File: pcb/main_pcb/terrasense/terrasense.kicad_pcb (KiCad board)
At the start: 4 copper layers, 100 x 80 mm, 79 parts, among them J1 SSR 0, J10 12V, J11 OneWire0, J12 12V In, J13 OneWire1, J14 OneWire2, J15 OneWire3, J16 OneWire4, J17 OneWire5, J18 I2C Mult 0, J19 I2C Mult 1, J2 SSR 1, J20 I2C Mult 2, J21 I2C Mult 3, J22 OneWire6, J23 OneWire7, J24 I2C Mult 4, J25 I2C Mult 5, J26 I2C_Debug, J27 ExtraIO, J3 SSR 2, J4 SSR 3, J5 FAN0, J6 FAN1, J7 XKZ-Y25-NPN, J8 SSR 0-3, J9 3V3, Q1 MMBT2222A, Q10 MMBT2222A, Q2 MMBT2222A, Q3 MMBT2222A, Q4 MMBT2222A, Q5 MMBT2222A, Q6 BSS84, Q7 MMBT2222A, Q8 MMBT2222A, Q9 BSS84, U1 ESP32-C6-DevKitC-1, U2 Mini560, U3 TCA9548APWR, U4 MPM3632CGQV-P

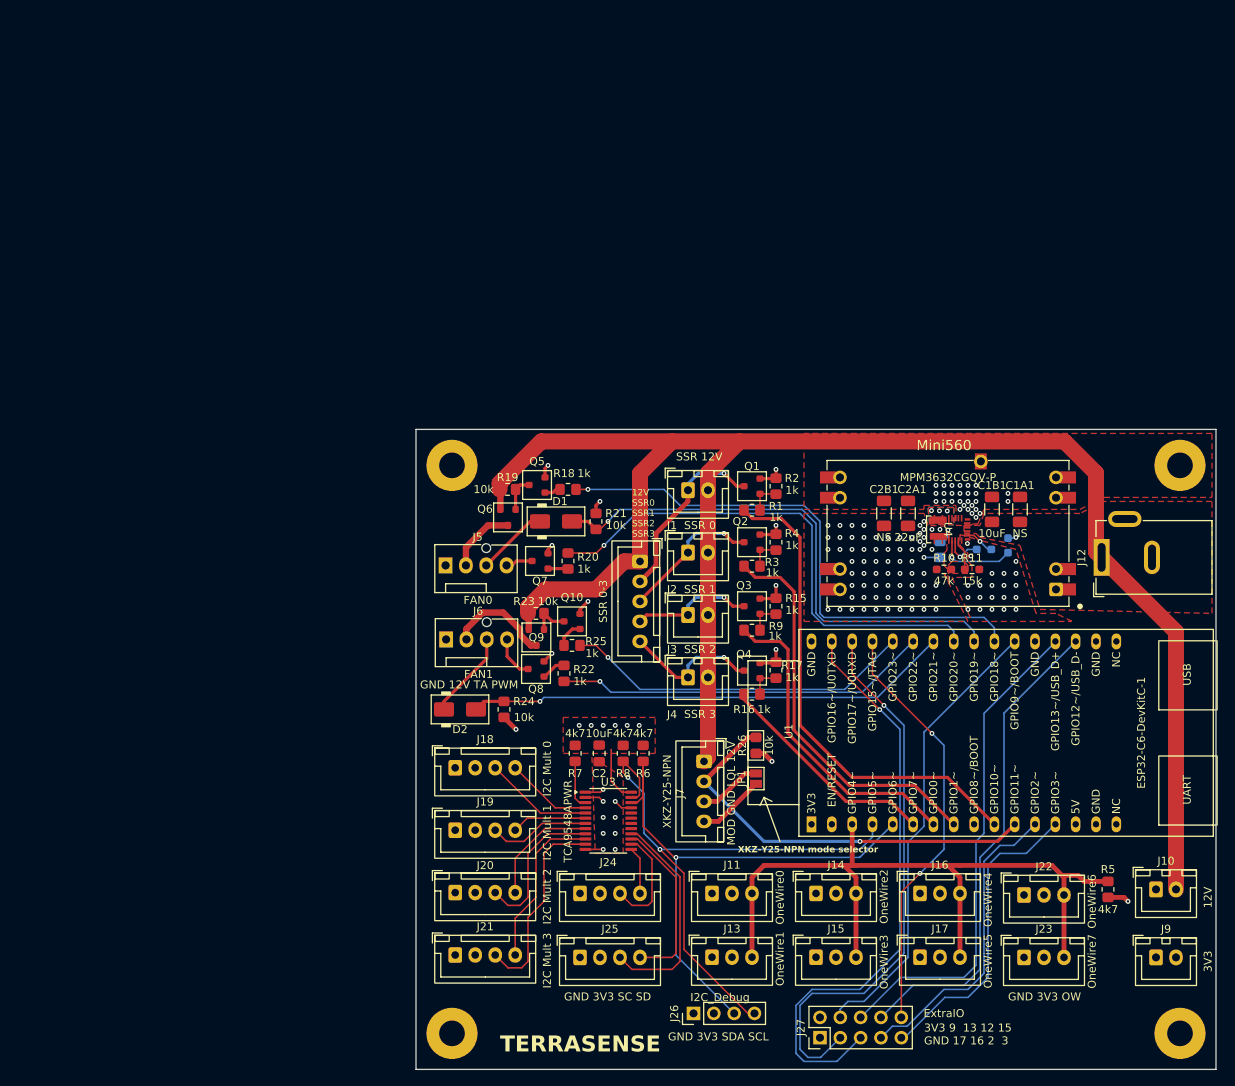
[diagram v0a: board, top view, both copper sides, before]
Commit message: update pcb with ordered pcb
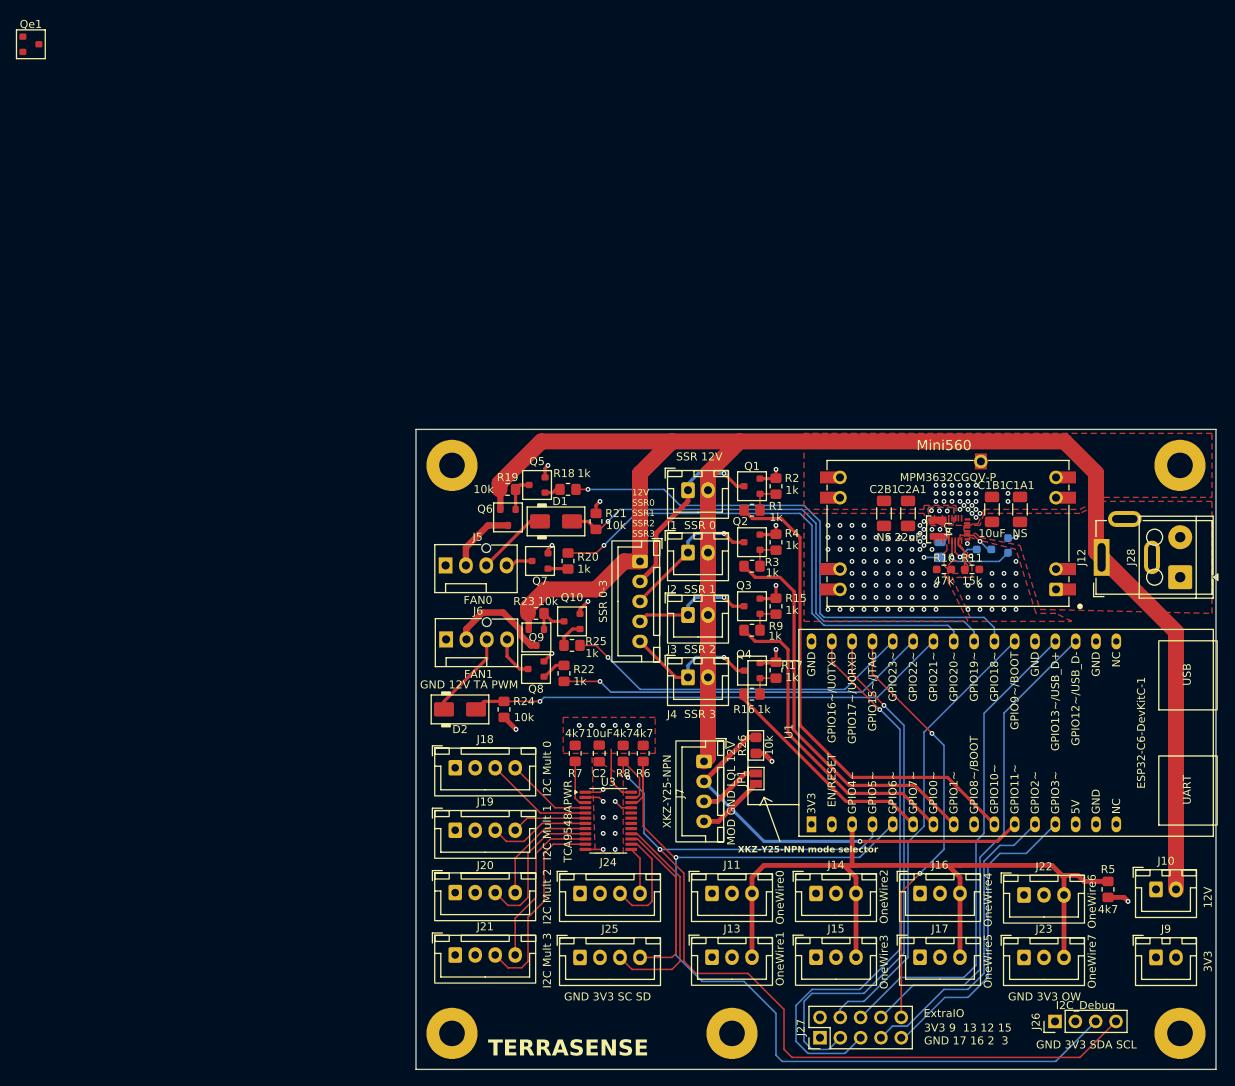
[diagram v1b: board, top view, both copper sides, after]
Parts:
- added J28: 12V_In, TerminalBlock_Altech:Altech_AK100_1x02_P5.00mm, F.Cu at (145.5, 68.5)
- added Qe1: A3401, PCM_Package_TO_SOT_SMD_AKL:SOT-23, F.Cu at (1.86, 1.86)
- added REF**: MH4, MountingHole:MountingHole_3.2mm_M3_Pad, F.Cu at (89.5, 125.5)
- Q6, Q9: value BSS84 -> A3401
- moved J26 45.2 mm to (129.9, 124.0)
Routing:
- net /I2C_MULT/I2C_SDA: track 73.8 -> 126.9 mm
- net /I2C_MULT/I2C_SCL: track 71.4 -> 124.2 mm
- net /GPIO17/U0RXD: track 69.3 -> 67.2 mm
- net /GPIO16/U0TXD: track 73.7 -> 72.0 mm
